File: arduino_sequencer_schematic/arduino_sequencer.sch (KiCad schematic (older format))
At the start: 178 parts, among them J1 AudioJack, J10 AudioJack, J11 AudioJack, J12 AudioJack, J13 AudioJack, J14 AudioJack, J15 AudioJack, J16 Conn_02x05, J17 Conn_01x03, J2 AudioJack, J3 AudioJack, J4 AudioJack, J5 AudioJack, J6 AudioJack, J7 AudioJack, J8 AudioJack, J9 AudioJack, Q1 2N3904, Q10 2N3904, Q11 2N3904, Q2 2N3904, Q3 2N3904, Q4 2N3904, Q5 2N3904, Q6 2N3904, Q7 2N3904, Q8 2N3904, Q9 2N3904, SW1 SW_SPST, SW2 SW_Push, SW3 SW_Push, SW4 SW_Push, SW5 SW_SPST, SW6 SW_SPST, U1 L78L09_TO92, U2 74HC595, U3 TL084, U4 TL084, U5 L7805

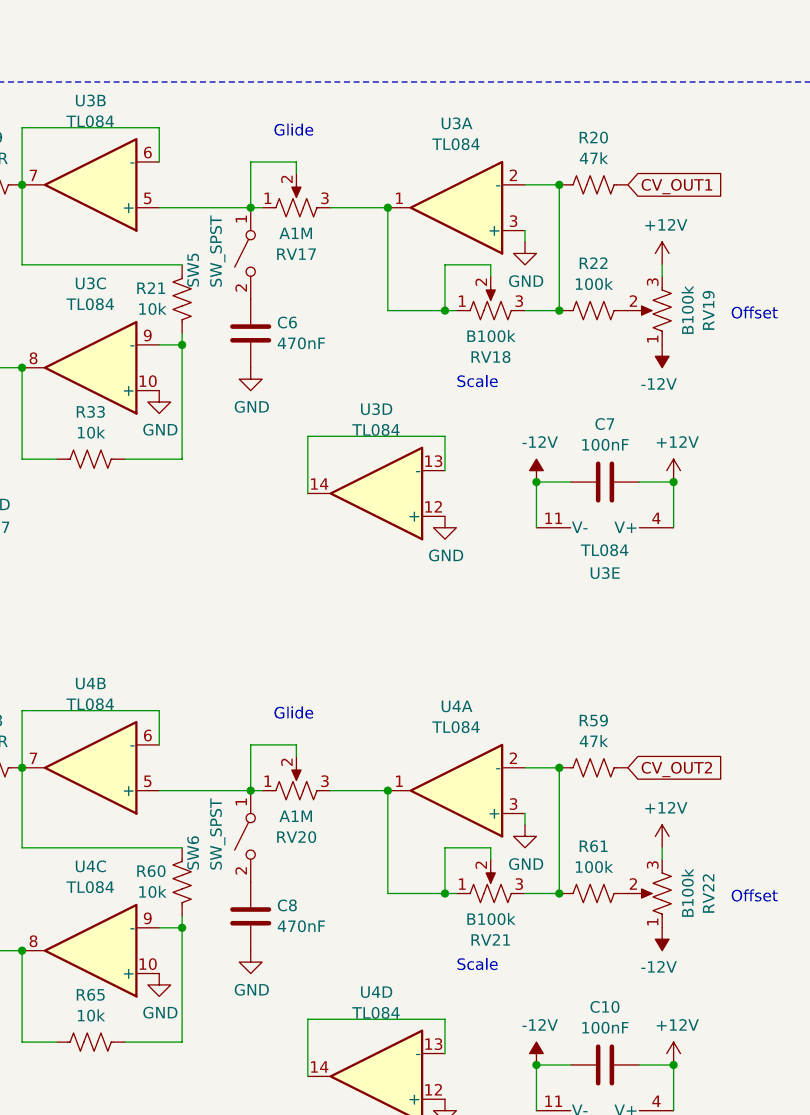
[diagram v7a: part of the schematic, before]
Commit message: Fixed potentiometer directions
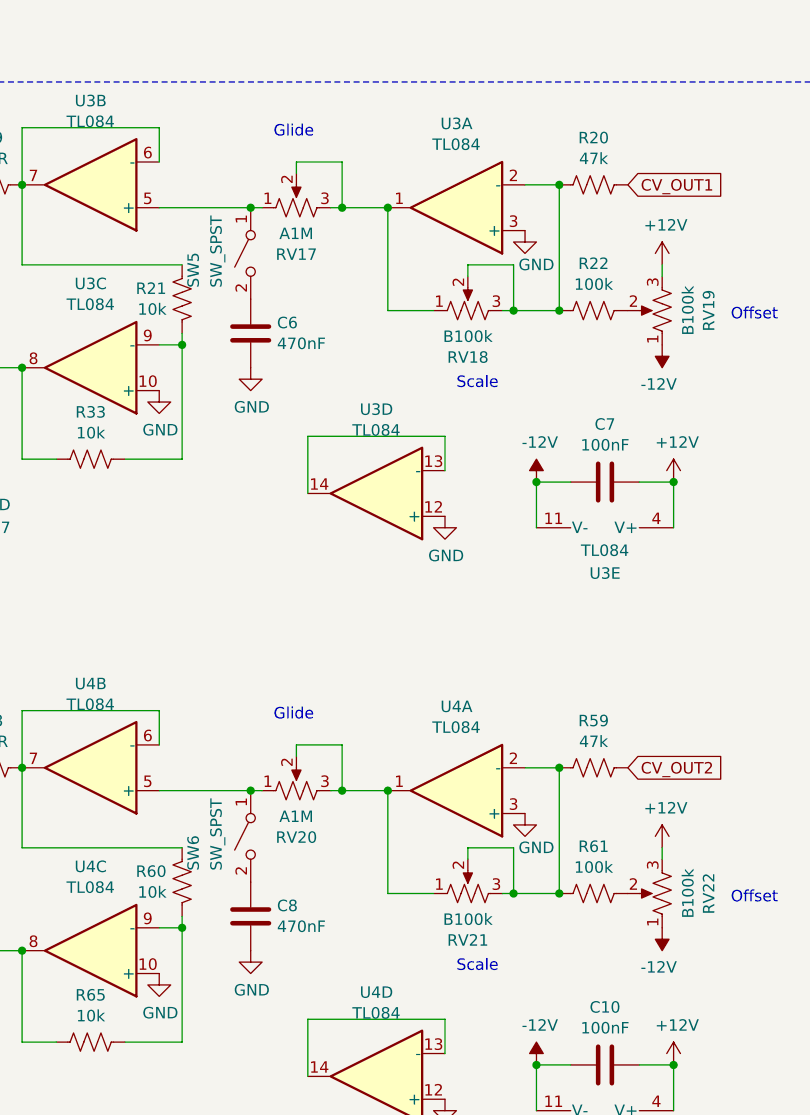
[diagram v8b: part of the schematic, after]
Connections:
- net at RV20.3, RV21.1, U4.1: now also RV20.2; no longer RV21.2
- net at R59.2, R61.2, RV21.3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: now also RV21.2
- net at RV20.1, SW6.1 (A), U4.5 (+): no longer RV20.2
- net at RV17.3, RV18.1, U3.1: now also RV17.2; no longer RV18.2
- net at R20.2, R22.2, RV18.3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: now also RV18.2
- net at RV17.1, SW5.1 (A), U3.5 (+): no longer RV17.2
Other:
- moved on the sheet: RV18, RV21
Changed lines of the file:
@@
 	1    0    0    -1
 $EndComp
-Wire Wire Line
-	4350 9000 4350 8950
 $Comp
 L power:GND #PWR064
 U 1 1 60918D15
-P 4350 9000
-F 0 "#PWR064" H 4350 8750 50  0001 C CNN
-F 1 "GND" H 4355 8827 50  0000 C CNN
-F 2 "" H 4350 9000 50  0001 C CNN
-F 3 "" H 4350 9000 50  0001 C CNN
-	1    4350 9000
+P 4350 8950
+F 0 "#PWR064" H 4350 8700 50  0001 C CNN
+F 1 "GND" H 4400 8800 50  0000 C CNN
+F 2 "" H 4350 8950 50  0001 C CNN
+F 3 "" H 4350 8950 50  0001 C CNN
+	1    4350 8950
 	1    0    0    -1
 $EndComp
@@
 L Device:R_POT_US RV21
 U 1 1 60985B51
-P 4200 9300
-F 0 "RV21" V 3995 9300 50  0000 C CNN
-F 1 "B100k" V 4086 9300 50  0000 C CNN
-F 2 "Potentiometer_THT:Potentiometer_Alpha_RD901F-40-00D_Single_Vertical" H 4200 9300 50  0001 C CNN
-F 3 "~" H 4200 9300 50  0001 C CNN
-	1    4200 9300
+P 4100 9300
+F 0 "RV21" V 3895 9300 50  0000 C CNN
+F 1 "B100k" V 3986 9300 50  0000 C CNN
+F 2 "Potentiometer_THT:Potentiometer_Alpha_RD901F-40-00D_Single_Vertical" H 4100 9300 50  0001 C CNN
+F 3 "~" H 4100 9300 50  0001 C CNN
+	1    4100 9300
 	0    -1   -1   0
 $EndComp
 Wire Wire Line
-	4050 9300 4000 9300
-Connection ~ 4000 9300
-Wire Wire Line
-	3750 9300 4000 9300
-Wire Wire Line
-	4350 9300 4500 9300
+	4250 9300 4300 9300
 $Comp
 L Device:R_POT_US RV20
@@
 	3350 8700 3350 8650
 Wire Wire Line
-	3350 8650 3150 8650
-Wire Wire Line
-	3150 8650 3150 8850
-Wire Wire Line
 	3150 8850 3200 8850
 $Comp
@@
 NoConn ~ 1500 9650
 Wire Wire Line
-	4000 9100 4000 9300
-Wire Wire Line
-	4000 9100 4200 9100
-Wire Wire Line
-	4200 9100 4200 9150
+	4100 9100 4100 9150
 Text GLabel 4800 8750 2    50   Input ~ 0
 CV_OUT2
@@
 	3750 8850 3750 9300
 Wire Wire Line
-	3750 8850 3500 8850
+	3750 8850 3550 8850
 Connection ~ 3750 8850
 $Comp
@@
 	1    0    0    -1
 $EndComp
-Wire Wire Line
-	4350 6450 4350 6400
 $Comp
 L power:GND #PWR029
 U 1 1 6126E46D
-P 4350 6450
-F 0 "#PWR029" H 4350 6200 50  0001 C CNN
-F 1 "GND" H 4355 6277 50  0000 C CNN
-F 2 "" H 4350 6450 50  0001 C CNN
-F 3 "" H 4350 6450 50  0001 C CNN
-	1    4350 6450
+P 4350 6400
+F 0 "#PWR029" H 4350 6150 50  0001 C CNN
+F 1 "GND" H 4400 6250 50  0000 C CNN
+F 2 "" H 4350 6400 50  0001 C CNN
+F 3 "" H 4350 6400 50  0001 C CNN
+	1    4350 6400
 	1    0    0    -1
 $EndComp
@@
 L Device:R_POT_US RV18
 U 1 1 6126E473
-P 4200 6750
-F 0 "RV18" V 3995 6750 50  0000 C CNN
-F 1 "B100k" V 4086 6750 50  0000 C CNN
-F 2 "Potentiometer_THT:Potentiometer_Alpha_RD901F-40-00D_Single_Vertical" H 4200 6750 50  0001 C CNN
-F 3 "~" H 4200 6750 50  0001 C CNN
-	1    4200 6750
+P 4100 6750
+F 0 "RV18" V 3895 6750 50  0000 C CNN
+F 1 "B100k" V 3986 6750 50  0000 C CNN
+F 2 "Potentiometer_THT:Potentiometer_Alpha_RD901F-40-00D_Single_Vertical" H 4100 6750 50  0001 C CNN
+F 3 "~" H 4100 6750 50  0001 C CNN
+	1    4100 6750
 	0    -1   -1   0
 $EndComp
 Wire Wire Line
-	4050 6750 4000 6750
-Connection ~ 4000 6750
-Wire Wire Line
-	3750 6750 4000 6750
-Wire Wire Line
-	4350 6750 4500 6750
+	4250 6750 4300 6750
 $Comp
 L Device:R_POT_US RV17
@@
 	3350 6150 3350 6100
 Wire Wire Line
-	3350 6100 3150 6100
-Wire Wire Line
-	3150 6100 3150 6300
-Wire Wire Line
 	3150 6300 3200 6300
 $Comp
@@
 NoConn ~ 1500 6300
 NoConn ~ 1500 7100
-Wire Wire Line
-	4000 6550 4000 6750
-Wire Wire Line
-	4000 6550 4200 6550
-Wire Wire Line
-	4200 6550 4200 6600
 Text GLabel 4800 6200 2    50   Input ~ 0
 CV_OUT1
@@
 	3750 6300 3750 6750
 Wire Wire Line
-	3750 6300 3500 6300
+	3750 6300 3550 6300
 Connection ~ 3750 6300
 Text Notes 5250 6800 0    50   ~ 0
@@
 Connection ~ 3100 1350
 Connection ~ 2950 1350
+Wire Wire Line
+	3350 6100 3550 6100
+Wire Wire Line
+	3550 6100 3550 6300
+Connection ~ 3550 6300
+Wire Wire Line
+	3550 6300 3500 6300
+Wire Wire Line
+	3350 8650 3550 8650
+Wire Wire Line
+	3550 8650 3550 8850
+Connection ~ 3550 8850
+Wire Wire Line
+	3550 8850 3500 8850
+Wire Wire Line
+	3750 9300 3950 9300
+Wire Wire Line
+	4300 9100 4300 9300
+Connection ~ 4300 9300
+Wire Wire Line
+	4300 9300 4500 9300
+Wire Wire Line
+	4100 9100 4300 9100
+Wire Wire Line
+	3750 6750 3950 6750
+Wire Wire Line
+	4100 6600 4100 6550
+Wire Wire Line
+	4100 6550 4300 6550
+Wire Wire Line
+	4300 6550 4300 6750
+Connection ~ 4300 6750
+Wire Wire Line
+	4300 6750 4500 6750
 $EndSCHEMATC
